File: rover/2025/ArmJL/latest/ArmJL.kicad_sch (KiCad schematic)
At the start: 0 parts

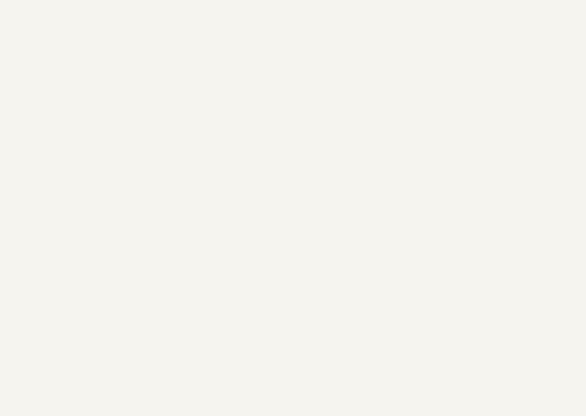
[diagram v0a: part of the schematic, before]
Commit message: ArmJ2 revised for order
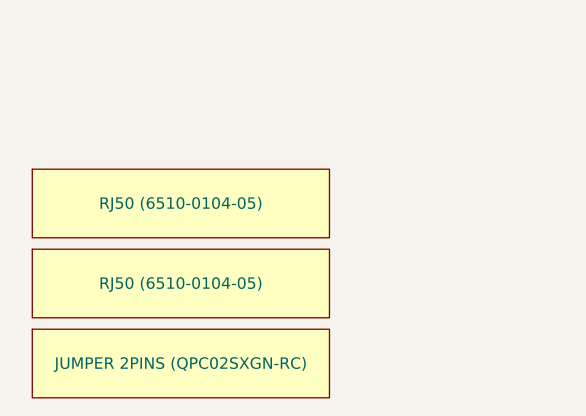
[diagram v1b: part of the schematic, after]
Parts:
- added G1: JUMPER 2PINS (QPC02SXGN-RC), symbol RoverLibrary:Off Board Part
- added G2, G3: RJ50 (6510-0104-05), symbol RoverLibrary:Off Board Part
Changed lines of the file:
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@@
+		)
+	)
+	(symbol
+		(lib_name "Off Board Part_1")
+		(lib_id "RoverLibrary:Off Board Part")
+		(at 30.48 191.77 0)
+		(unit 1)
+		(exclude_from_sim yes)
+		(in_bom yes)
+		(on_board no)
+		(dnp no)
+		(fields_autoplaced yes)
+		(property "Reference" "G1"
+			(at 30.48 149.9301 0)
+			(effects
+				(font
+					(size 1.27 1.27)
+				)
+				(hide yes)
+			)
+		)
+		(property "Value" "JUMPER 2PINS (QPC02SXGN-RC)"
+			(at 30.48 191.77 0)
+			(effects
+				(font
+					(size 1.27 1.27)
+				)
+			)
+		)
+		(property "Footprint" ""
+			(at 27.94 190.5 0)
+			(effects
+				(font
+					(size 1.27 1.27)
+				)
+				(hide yes)
+			)
+		)
+		(property "Datasheet" ""
+			(at 27.94 190.5 0)
+			(effects
+				(font
+					(size 1.27 1.27)
+				)
+				(hide yes)
+			)
+		)
+		(property "Description" ""
+			(at 27.94 190.5 0)
+			(effects
+				(font
+					(size 1.27 1.27)
+				)
+				(hide yes)
+			)
+		)
+		(property "Digikey" "https://www.digikey.ca/en/products/detail/sullins-connector-solutions/QPC02SXGN-RC/2618262"
+			(at 30.48 191.77 0)
+			(effects
+				(font
+					(size 1.27 1.27)
+				)
+				(hide yes)
+			)
+		)
+		(instances
+			(project "ArmJL"
+				(path "/ea96555f-a650-48ef-b94f-b65180d69193"
+					(reference "G1")
+					(unit 1)
+				)
+			)
+		)
+	)
+	(symbol
+		(lib_name "Off Board Part_1")
+		(lib_id "RoverLibrary:Off Board Part")
+		(at 30.48 173.99 0)
+		(unit 1)
+		(exclude_from_sim yes)
+		(in_bom yes)
+		(on_board no)
+		(dnp no)
+		(fields_autoplaced yes)
+		(property "Reference" "G3"
+			(at 30.48 132.1501 0)
+			(effects
+				(font
+					(size 1.27 1.27)
+				)
+				(hide yes)
+			)
+		)
+		(property "Value" "RJ50 (6510-0104-05)"
+			(at 30.48 173.99 0)
+			(effects
+				(font
+					(size 1.27 1.27)
+				)
+			)
+		)
+		(property "Footprint" ""
+			(at 27.94 172.72 0)
+			(effects
+				(font
+					(size 1.27 1.27)
+				)
+				(hide yes)
+			)
+		)
+		(property "Datasheet" ""
+			(at 27.94 172.72 0)
+			(effects
+				(font
+					(size 1.27 1.27)
+				)
+				(hide yes)
+			)
+		)
+		(property "Description" ""
+			(at 27.94 172.72 0)
+			(effects
+				(font
+					(size 1.27 1.27)
+				)
+				(hide yes)
+			)
+		)
+		(property "Digikey" "https://www.digikey.ca/en/products/detail/encitech-connectors-ab/6510-0104-05/25596593"
+			(at 30.48 173.99 0)
+			(effects
+				(font
+					(size 1.27 1.27)
+				)
+				(hide yes)
+			)
+		)
+		(instances
+			(project "ArmJL"
+				(path "/ea96555f-a650-48ef-b94f-b65180d69193"
+					(reference "G3")
+					(unit 1)
+				)
+			)
+		)
+	)
+	(symbol
+		(lib_name "Off Board Part_1")
+		(lib_id "RoverLibrary:Off Board Part")
+		(at 30.48 182.88 0)
+		(unit 1)
+		(exclude_from_sim yes)
+		(in_bom yes)
+		(on_board no)
+		(dnp no)
+		(fields_autoplaced yes)
+		(property "Reference" "G2"
+			(at 30.48 141.0401 0)
+			(effects
+				(font
+					(size 1.27 1.27)
+				)
+				(hide yes)
+			)
+		)
+		(property "Value" "RJ50 (6510-0104-05)"
+			(at 30.48 182.88 0)
+			(effects
+				(font
+					(size 1.27 1.27)
+				)
+			)
+		)
+		(property "Footprint" ""
+			(at 27.94 181.61 0)
+			(effects
+				(font
+					(size 1.27 1.27)
+				)
+				(hide yes)
+			)
+		)
+		(property "Datasheet" ""
+			(at 27.94 181.61 0)
+			(effects
+				(font
+					(size 1.27 1.27)
+				)
+				(hide yes)
+			)
+		)
+		(property "Description" ""
+			(at 27.94 181.61 0)
+			(effects
+				(font
+					(size 1.27 1.27)
+				)
+				(hide yes)
+			)
+		)
+		(property "Digikey" "https://www.digikey.ca/en/products/detail/encitech-connectors-ab/6510-0104-05/25596593"
+			(at 30.48 182.88 0)
+			(effects
+				(font
+					(size 1.27 1.27)
+				)
+				(hide yes)
+			)
+		)
+		(instances
+			(project "ArmJL"
+				(path "/ea96555f-a650-48ef-b94f-b65180d69193"
+					(reference "G2")
+					(unit 1)
+				)
+			)
 		)
 	)
@@
 		)
 		(instances
-			(project "ARM-JL"
+			(project "ArmJL"
 				(path "/ea96555f-a650-48ef-b94f-b65180d69193"
 					(page "2")
